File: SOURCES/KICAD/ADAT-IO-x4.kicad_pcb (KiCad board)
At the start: 2 copper layers, 200 x 100 mm, 95 parts, among them IC11 XC6SLX9-TQ144, IC12 AT25F2048N, IC13 LTC3419, IC14 74AHC14, IC20 ADM811TARTZ, SW1 NT04, SW2 5MS1, X1 PLR135/T10, X10 PLT133/T10W, X11 IDC-2x32, X12 IDC-2x8, X13 IDC-2x8, X2 PLR135/T10, X3 PLR135/T10, X4 PLR135/T10, X5 PLT133/T10W, X6 CONN_02X07, X7 BNC, X8 PLT133/T10W, X9 PLT133/T10W

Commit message: PCB layout prototype
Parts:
- removed C114: 100n, rklib:C0805-X7R
- removed D10, D9: 1N4148, Diodes_SMD:MiniMELF_Standard
- removed IC14: 74AHC14, Housings_SOIC:SOIC-14_3.9x8.7mm_Pitch1.27mm
- removed R64: 301R, rklib:C0805-RES
- removed R65: 100R, rklib:C0805-RES
- removed R66, R67: 51R1, rklib:C0805-RES
- removed R68: 1M00, rklib:C0805-RES
- removed SW2: 5MS1, rklib:5MS1-SPDT
- added B1: TEST_1P, Mounting_Holes:MountingHole_3mm, F.Cu at (105.0, 65.0)
- added B2: TEST_1P, Mounting_Holes:MountingHole_3mm, F.Cu at (195.0, 65.0)
- added B3: TEST_1P, Mounting_Holes:MountingHole_3mm, F.Cu at (195.0, 135.0)
- added B4: TEST_1P, Mounting_Holes:MountingHole_3mm, F.Cu at (105.0, 135.0)
- added C8: 10u0./63V, Capacitors_ThroughHole:C_Radial_D5_L11_P2, F.Cu at (184.4, 70.8)
- added C9: 10u0./63V, Capacitors_ThroughHole:C_Radial_D5_L11_P2, F.Cu at (184.4, 86.7)
- added IC1: LM1117-5.0, SOT-223, F.Cu at (185.4, 78.3)
- SW1: footprint rklib:NT04-H -> Buttons_Switches_ThroughHole:SW_DIP_x4_Slide
- X7: value BNC -> MM-6G; footprint rklib:BNC-H -> rklib:MM-6G
- moved X7 165.2 mm to (157.5, 118.1), turned to 0 degrees
- moved X8 139.1 mm to (144.0, 143.9)
- moved C83 137.5 mm to (120.0, 139.6)
- moved C7 88.9 mm to (191.0, 140.4), turned to 180 degrees
- moved L3 80.2 mm to (104.9, 140.4), turned to 180 degrees
- moved X1 78.8 mm to (108.0, 143.9)
- moved C1 76.6 mm to (108.4, 140.4)
- moved X9 75.3 mm to (168.0, 143.9)
- moved C6 72.5 mm to (168.0, 139.6), turned to 90 degrees
- moved L4 70.7 mm to (127.4, 139.6), turned to 90 degrees
- moved C2 69.5 mm to (129.4, 139.6), turned to 90 degrees
- moved X2 69.4 mm to (132.0, 143.9)
- moved X10 68.9 mm to (192.0, 143.9)
- moved L5 62.4 mm to (151.5, 139.6), turned to 90 degrees
- moved X3 60.1 mm to (156.0, 143.9)
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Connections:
- IC11 pad 101: (no net) -> /WCLKOUT
- IC11 pad 102: (no net) -> /WCLKIN
- IC11 pad 114: /WCLKIN -> (no net)
- IC11 pad 14: /SDA:3 -> /SCL:3
- IC11 pad 142: Net-(IC11-Pad142) -> /MDO:4
- IC11 pad 143: /MDO:4 -> Net-(IC11-Pad143)
- IC11 pad 15: /SCL:3 -> /SDA:3
- IC11 pad 24: /SDA:2 -> /SCL:2
- IC11 pad 26: /SCL:2 -> /SDA:2
- IC11 pad 34: /SDA:1 -> /SCL:1
- IC11 pad 35: /SCL:1 -> /SDA:1
- IC11 pad 6: /SDA:4 -> /SCL:4
- IC11 pad 7: /SCL:4 -> /SDA:4
- R1 pad 2: Net-(IC11-Pad142) -> Net-(IC11-Pad143)
- R58 pad 2: /SW:1 -> /SW:4
- R59 pad 2: /SW:2 -> /SW:3
- R60 pad 2: /SW:3 -> /SW:2
- R61 pad 2: /SW:4 -> /SW:1
- R8 pad 1: Net-(IC11-Pad33) -> (no net)
- R8 pad 2: Net-(IC11-Pad32) -> Net-(IC11-Pad33)
- R8 pad 3: (no net) -> Net-(IC11-Pad32)
- R8 pad 6: (no net) -> /LRCK:1
- R8 pad 7: /LRCK:1 -> /MCLK:1
- R8 pad 8: /MCLK:1 -> (no net)
- SW1 pad 5: /SW:4 -> /SW:1
- SW1 pad 6: /SW:3 -> /SW:2
- SW1 pad 7: /SW:2 -> /SW:3
- SW1 pad 8: /SW:1 -> /SW:4
- X7 pad 1: Net-(R66-Pad2) -> +3V3
- X7 pad 2: GND -> +5V
- X7 pad 3: (no net) -> /WCLKIN
- X7 pad 4: (no net) -> GND
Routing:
- net +3V3: track 439.9 -> 623.6 mm, vias 6 -> 27
- net +12V: track 0.00 -> 181.0 mm
- net (no net): track 86.2 -> 0.00 mm, vias 1 -> 0
- net /SW:2: track 97.9 -> 37.1 mm
- net /SDA:1: track 3.75 -> 62.5 mm
- net /ADATOUT:4: track 0.00 -> 55.9 mm
- net /SCL:1: track 3.54 -> 59.1 mm
- net /SDA:4: track 0.00 -> 53.1 mm
- net /ADATIN:1: track 0.00 -> 52.5 mm
- net /SDA:2: track 3.18 -> 54.0 mm
- net /MDO:4: track 0.00 -> 50.8 mm, vias 0 -> 2
- net /ADATIN:4: track 0.00 -> 50.6 mm
- net /SCL:4: track 0.00 -> 48.6 mm
- net /MCLK:6: track 0.00 -> 48.3 mm
- net /WCLKIN: track 53.4 -> 7.40 mm, vias 2 -> 0
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- added copper zone on F.Cu, net +3V3
- added copper zone on B.Cu, net GND
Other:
- board size 200 x 100 mm -> 100 x 100 mm

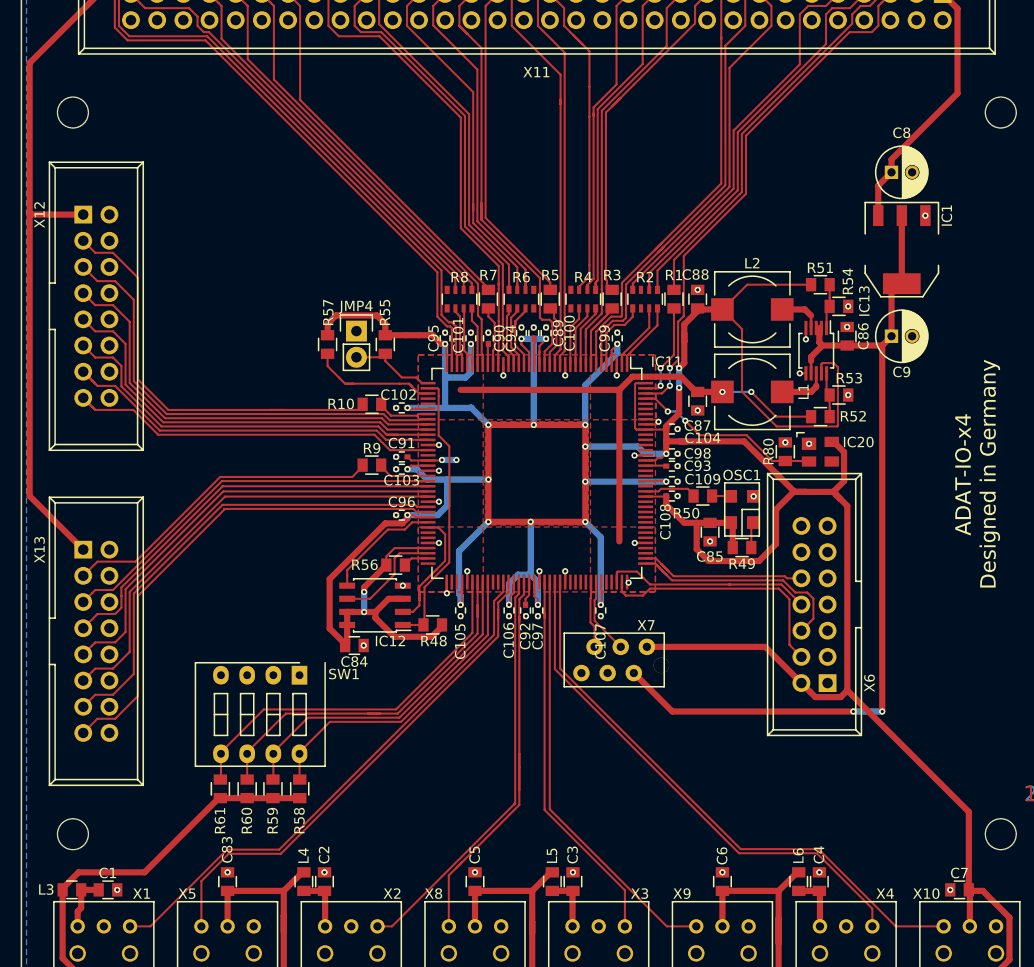
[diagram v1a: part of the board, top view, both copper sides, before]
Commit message: Reannotation
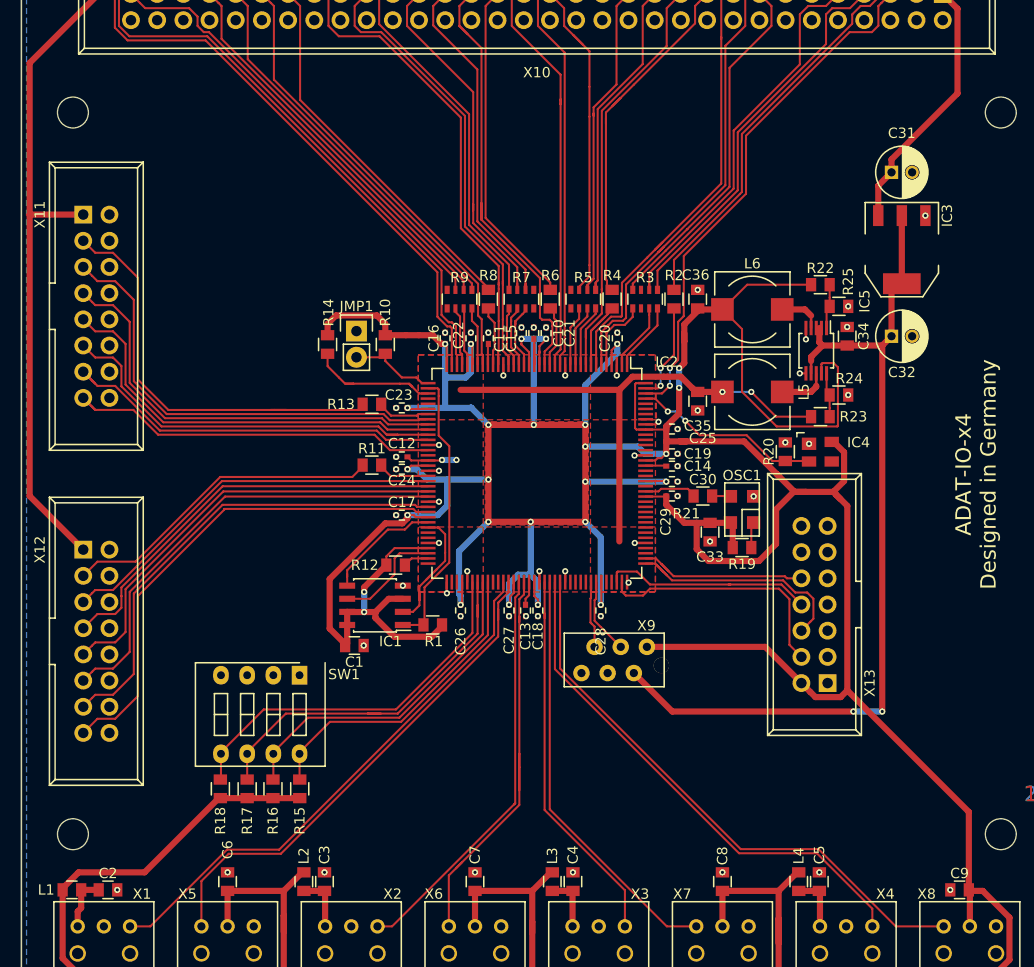
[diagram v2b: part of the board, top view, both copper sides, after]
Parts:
- renumbered C84 to C1, C89 to C10, C90 to C11, C91 to C12, C92 to C13, C93 to C14, C94 to C15, C95 to C16, C96 to C17, C97 to C18, C98 to C19, C1 to C2, C99 to C20, C100 to C21, C101 to C22, C102 to C23, C103 to C24, C104 to C25, C105 to C26, C106 to C27, C107 to C28, C108 to C29, C2 to C3, C109 to C30, C8 to C31, C9 to C32, C85 to C33, C86 to C34, C87 to C35, C88 to C36, C3 to C4, C4 to C5, C83 to C6, C5 to C7, C6 to C8, C7 to C9, IC12 to IC1, IC11 to IC2, IC1 to IC3, IC20 to IC4, IC13 to IC5, JMP4 to JMP1, L3 to L1, L4 to L2, L5 to L3, L6 to L4, L1 to L5, L2 to L6, R48 to R1, R55 to R10, R9 to R11, R56 to R12, R10 to R13, R57 to R14, R58 to R15, R59 to R16, R60 to R17, R61 to R18, R49 to R19, R1 to R2, R80 to R20, R50 to R21, R51 to R22, R52 to R23, R53 to R24, R54 to R25, R2 to R3, R3 to R4, R4 to R5, R5 to R6, R6 to R7, R7 to R8, R8 to R9, X11 to X10, X12 to X11, X13 to X12, X6 to X13, X8 to X6, X9 to X7, X10 to X8, X7 to X9

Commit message: Changed Termination
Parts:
- added R26: 33R0, Capacitors_SMD:C_0402, F.Cu at (146.2, 79.9)
- added R27: 33R0, Capacitors_SMD:C_0402, F.Cu at (145.0, 79.9)
- added R28: 33R0, Capacitors_SMD:C_0402, F.Cu at (144.1, 83.1)
- added R29: 33R0, Capacitors_SMD:C_0402, F.Cu at (153.3, 80.2)
- added R30: 33R0, Capacitors_SMD:C_0402, F.Cu at (152.1, 80.2)
- added R31: 33R0, Capacitors_SMD:C_0402, F.Cu at (150.5, 83.1)
- added R32: 33R0, Capacitors_SMD:C_0402, F.Cu at (139.3, 83.1)
- added R33: 33R0, Capacitors_SMD:C_0402, F.Cu at (138.1, 83.1)
- added R34: 33R0, Capacitors_SMD:C_0402, F.Cu at (159.7, 80.2)
- added R35: 33R0, Capacitors_SMD:C_0402, F.Cu at (158.5, 80.2)
- added R36: 33R0, Capacitors_SMD:C_0402, F.Cu at (156.9, 83.1)
- added R37: 33R0, Capacitors_SMD:C_0402, F.Cu at (164.5, 83.1)
- added R38: 33R0, Resistors_SMD:R_Array_Convex_4x0603, F.Cu at (133.6, 93.6)
- added R39: 33R0, Capacitors_SMD:C_0402, F.Cu at (133.6, 98.4)
- added R40: 33R0, Capacitors_SMD:C_0402, F.Cu at (133.6, 96.0)
- added R41: 33R0, Capacitors_SMD:C_0402, F.Cu at (133.6, 97.2)
- added R42: 33R0, Resistors_SMD:R_Array_Convex_4x0603, F.Cu at (133.6, 102.0)
- added R43: 33R0, Capacitors_SMD:C_0402, F.Cu at (133.6, 104.4)
- added R44: 33R0, Capacitors_SMD:C_0402, F.Cu at (133.6, 105.6)
- added R45: 33R0, Capacitors_SMD:C_0402, F.Cu at (133.6, 106.8)
- R11, R13, R2, R4, R6, R8: footprint rklib:C0805-RES -> Capacitors_SMD:C_0402
- moved C32 17.5 mm to (194.7, 72.6), turned to 90 degrees
- moved C34 15.5 mm to (195.0, 82.4)
- moved C35 15.5 mm to (180.5, 88.7)
- moved C36 15.5 mm to (180.5, 78.8)
- moved IC5 15.5 mm to (192.0, 83.8)
- moved L5 15.5 mm to (185.8, 87.8)
- moved L6 15.5 mm to (185.8, 79.8)
- moved R22 15.5 mm to (192.4, 77.4)
- moved R23 15.5 mm to (192.4, 90.2)
- moved R24 15.5 mm to (194.2, 88.1)
- moved R25 15.5 mm to (194.2, 79.5)
- moved IC3 6.76 mm to (186.3, 71.6), turned to 270 degrees
- moved C31 5.88 mm to (178.8, 72.6), turned to 90 degrees
- moved R13 3.04 mm to (136.9, 92.4)
- moved R9 0.80 mm to (141.7, 83.1)
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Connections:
- IC2 pad 14: /SCL:3 -> Net-(IC2-Pad14)
- IC2 pad 142: /MDO:4 -> Net-(IC2-Pad142)
- IC2 pad 15: /SDA:3 -> Net-(IC2-Pad15)
- IC2 pad 17: /MDO:2 -> Net-(IC2-Pad17)
- IC2 pad 24: /SCL:2 -> Net-(IC2-Pad24)
- IC2 pad 26: /SDA:2 -> Net-(IC2-Pad26)
- IC2 pad 29: /MDO:1 -> Net-(IC2-Pad29)
- IC2 pad 34: /SCL:1 -> Net-(IC2-Pad34)
- IC2 pad 35: /SDA:1 -> Net-(IC2-Pad35)
- IC2 pad 41: (no net) -> Net-(IC2-Pad41)
- IC2 pad 44: /MDO:5 -> Net-(IC2-Pad44)
- IC2 pad 45: /BCLK:5 -> Net-(IC2-Pad45)
- IC2 pad 46: /LRCK:5 -> (no net)
- IC2 pad 47: /SDA:5 -> Net-(IC2-Pad47)
- IC2 pad 48: /SCL:5 -> Net-(IC2-Pad48)
- IC2 pad 50: /MCLK:5 -> Net-(IC2-Pad50)
- IC2 pad 56: /MDO:6 -> Net-(IC2-Pad56)
- IC2 pad 57: /BCLK:6 -> Net-(IC2-Pad57)
- IC2 pad 58: /LRCK:6 -> Net-(IC2-Pad58)
- IC2 pad 59: /SDA:6 -> Net-(IC2-Pad59)
- IC2 pad 6: /SCL:4 -> Net-(IC2-Pad6)
- IC2 pad 61: /SCL:6 -> Net-(IC2-Pad61)
- IC2 pad 62: /MCLK:6 -> Net-(IC2-Pad62)
- IC2 pad 7: /SDA:4 -> Net-(IC2-Pad7)
- IC2 pad 9: /MDO:3 -> Net-(IC2-Pad9)
- R13 pad 1: Net-(IC2-Pad43) -> Net-(IC2-Pad41)
- R3 pad 1: Net-(IC2-Pad5) -> (no net)
- R3 pad 2: (no net) -> Net-(IC2-Pad5)
- R3 pad 7: (no net) -> /MCLK:4
- R3 pad 8: /MCLK:4 -> (no net)
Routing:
- net +5V: track 84.6 -> 103.7 mm
- net +1V2: track 67.6 -> 83.5 mm
- net /SCL:4: track 48.6 -> 36.9 mm
- net Net-(IC2-Pad142): track 0.00 -> 11.6 mm, vias 0 -> 2
- net Net-(IC2-Pad7): track 0.00 -> 11.3 mm
- net /MDO:2: track 45.2 -> 34.0 mm
- net Net-(IC2-Pad6): track 0.00 -> 11.0 mm
- net /SDA:3: track 49.0 -> 38.4 mm
- net /SDA:4: track 53.1 -> 42.5 mm
- net Net-(IC2-Pad26): track 0.00 -> 10.4 mm
- net /SCL:3: track 42.2 -> 32.5 mm
- net Net-(IC2-Pad24): track 0.00 -> 9.43 mm
- net /SDA:2: track 54.0 -> 44.6 mm
- net Net-(IC2-Pad14): track 0.00 -> 9.13 mm
- net Net-(IC2-Pad15): track 0.00 -> 9.05 mm
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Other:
- board text added: "ADAT-IO-x4 rev. A Designed in Germany"
- board text removed: "ADAT-IO-x4 Designed in Germany"
